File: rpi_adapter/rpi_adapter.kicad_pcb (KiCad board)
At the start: 2 copper layers, 40 x 55 mm, 5 parts, among them J1 Conn_02x20_Counter_Clockwise, J2 Conn_01x03, U1 RaspberryPi_Pico

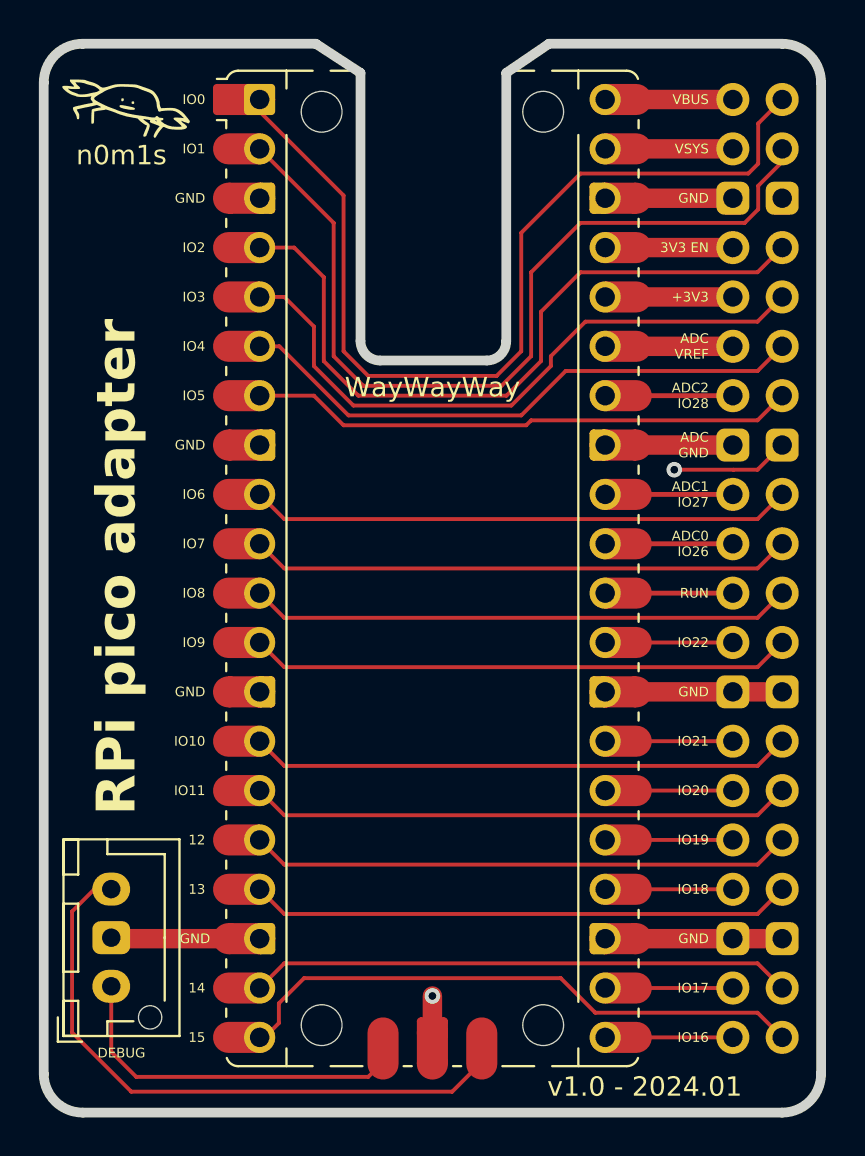
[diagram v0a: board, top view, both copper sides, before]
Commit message: Fix DRC + output gerber files
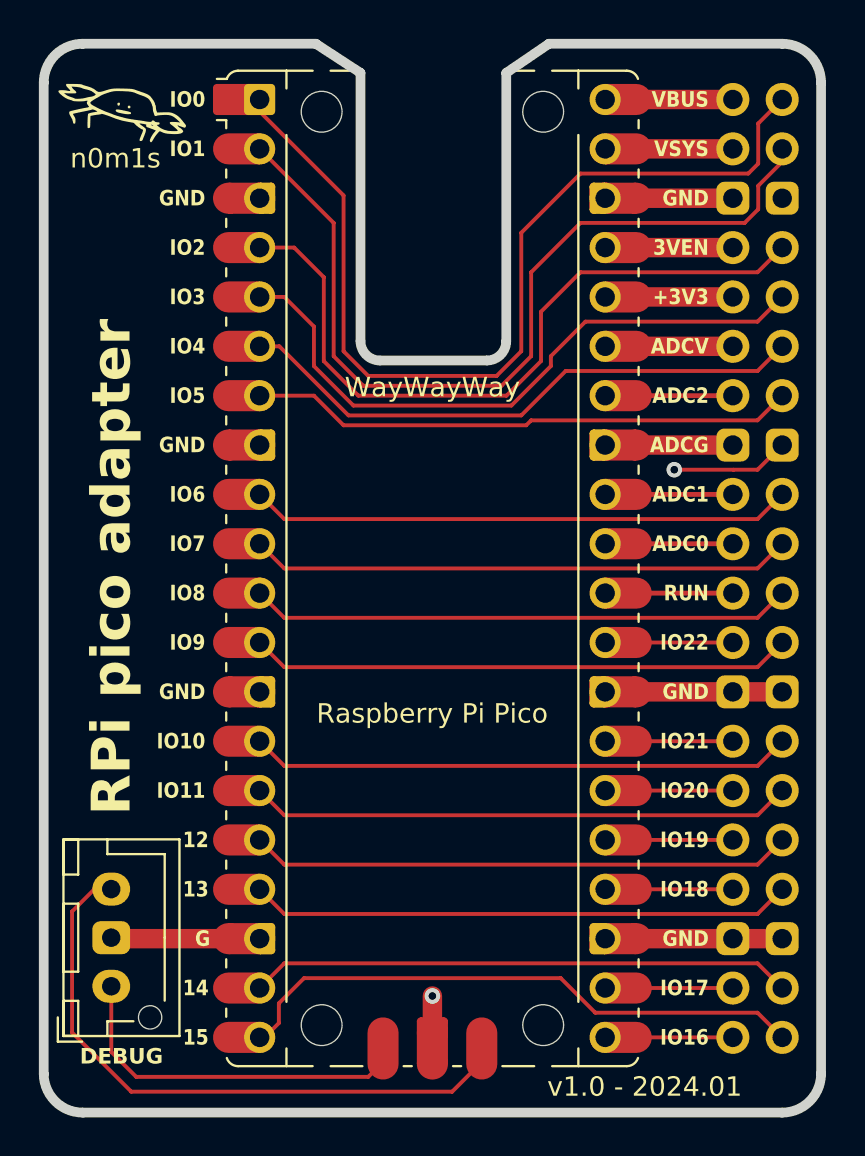
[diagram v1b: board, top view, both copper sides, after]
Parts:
- moved G*** 0.30 mm to (122.3, 83.9)
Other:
- board text added: "3VEN"
- board text added: "ADC0"
- board text added: "ADC1"
- board text added: "ADC2"
- board text added: "ADCG"
- board text added: "ADCV"
- board text added: "G"
- board text added: "Raspberry Pi Pico"
- board text removed: "3V3 EN"
- board text removed: "ADC GND"
- board text removed: "ADC VREF"
- board text removed: "ADC0 IO26"
- board text removed: "ADC1 IO27"
- board text removed: "ADC2 IO28"
